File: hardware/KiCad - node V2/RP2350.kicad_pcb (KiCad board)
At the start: 4 copper layers, 56 x 32 mm, 82 parts, among them J3 USB_C_Receptacle_USB2.0_14P, SW1 BOOTSEL, U1 RP2350A, U2 THVD1450D, U3 ADXL355BEZ, U4 TPS2121RUXR, U5 USBLC6-2SC6, U6 TLV75733PDBV, U7 W25Q128JVS, U8 TPS7A20xxxDBV

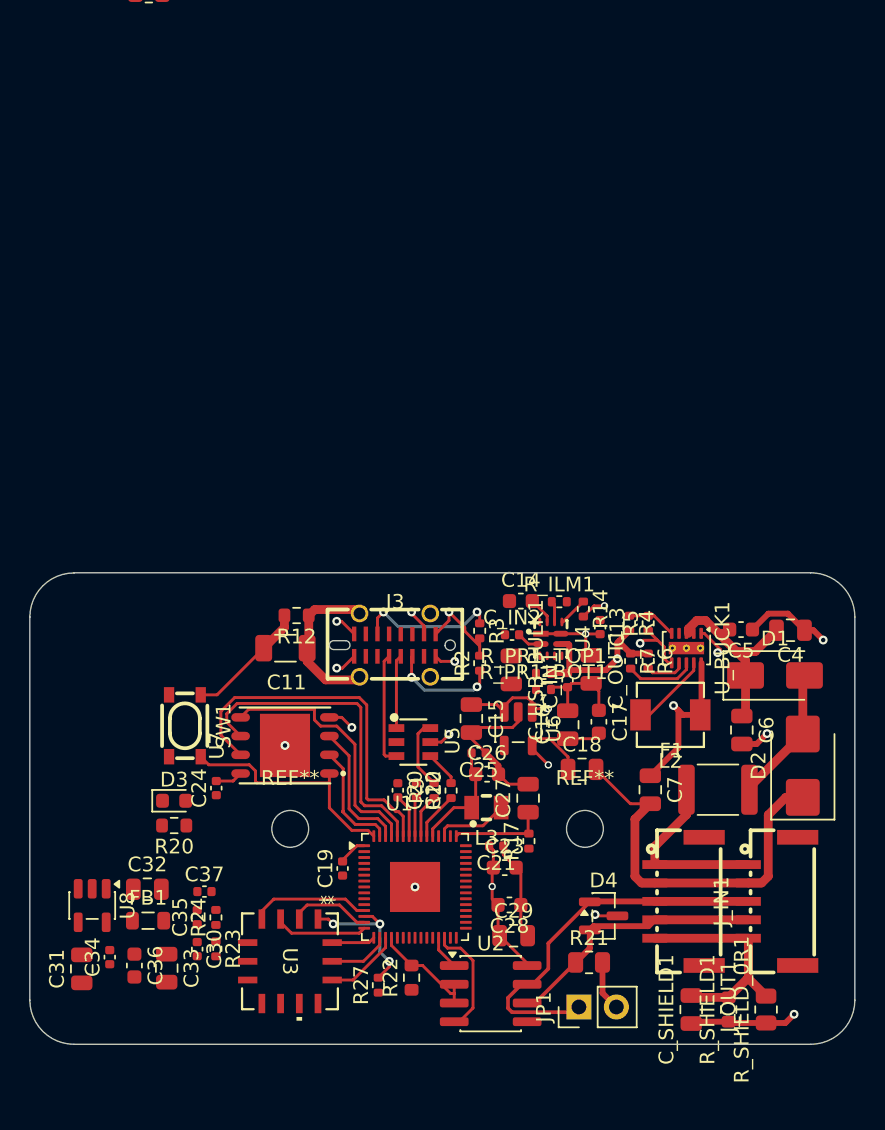
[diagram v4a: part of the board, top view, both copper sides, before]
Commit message: hardware: pico pin change, moved mounting holes
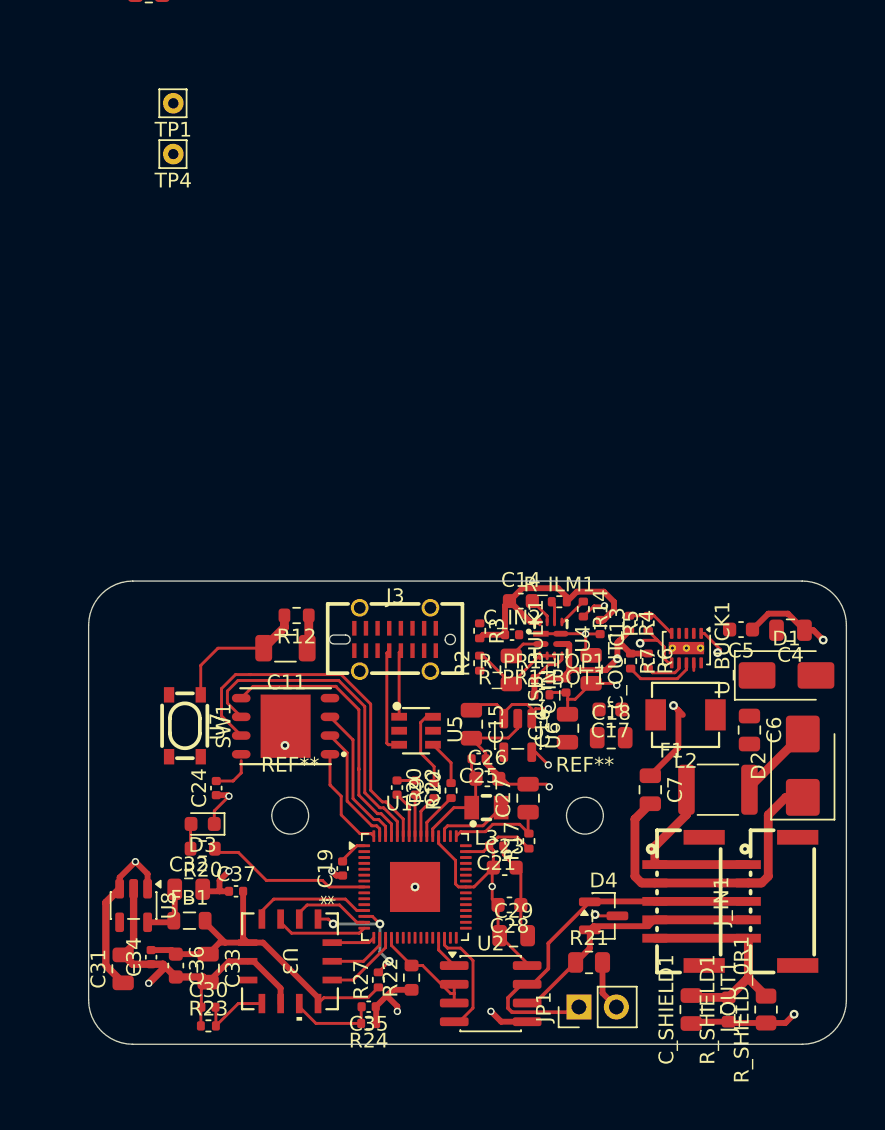
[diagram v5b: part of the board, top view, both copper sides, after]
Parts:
- added TP1: 5V_SYS, Connector_Pin:Pin_D0.7mm_L6.5mm_W1.8mm_FlatFork, F.Cu at (128.3, 45.7)
- added TP4: 12V_Protected, Connector_Pin:Pin_D0.7mm_L6.5mm_W1.8mm_FlatFork, F.Cu at (128.3, 49.1)
- moved C35 13.1 mm to (141.6, 107.0), turned to 180 degrees
- moved R24 12.6 mm to (141.6, 108.1), turned to 180 degrees
- moved R23 5.26 mm to (130.7, 108.3), turned to 0 degrees
- moved C30 4.01 mm to (130.7, 107.0), turned to 0 degrees
- moved C18 2.92 mm to (158.0, 88.7)
- moved C31 2.81 mm to (124.9, 104.4)
- moved C34 2.81 mm to (126.8, 103.6)
- moved FB1 2.81 mm to (129.4, 101.2)
- moved U8 2.81 mm to (125.6, 100.1)
- moved C32 2.81 mm to (129.3, 99.0)
- moved C33 2.81 mm to (130.7, 104.4)
- moved C36 2.81 mm to (128.5, 104.2)
- moved D3 2.50 mm to (130.3, 94.6), turned to 180 degrees
- moved R20 2.50 mm to (130.3, 96.3)
- moved C37 2.14 mm to (132.6, 99.2)
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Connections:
- net /12V_BUS renamed /12V
- net Net-(U1-QSPI_SD1) renamed /DO
- net Net-(U1-QSPI_SD2) renamed /WP
- net Net-(U1-USB_DM) renamed /USB_DM
- net Net-(U1-USB_DP) renamed /USB_DP
- net Net-(U1-~{QSPI_SS}) renamed /CS
- R20 pad 1: Net-(U1-GPIO25) -> Net-(U1-GPIO5)
- R22 pad 2: Net-(U1-GPIO15) -> Net-(U1-GPIO18)
- U1 pad 19: Net-(U1-GPIO15) -> unconnected-(U1-GPIO15-Pad19)
- U1 pad 29: unconnected-(U1-GPIO18-Pad29) -> Net-(U1-GPIO18)
- U1 pad 37: Net-(U1-GPIO25) -> unconnected-(U1-GPIO25-Pad37)
- U1 pad 8: unconnected-(U1-GPIO5-Pad8) -> Net-(U1-GPIO5)
- U2 pad 2: Net-(U1-GPIO15) -> Net-(U1-GPIO18)
- U2 pad 3: Net-(U1-GPIO15) -> Net-(U1-GPIO18)
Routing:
- net /5V_SYS: track 18.7 -> 78.3 mm, vias 2 -> 3
- net GND: track 94.1 -> 141.8 mm, vias 13 -> 15
- net /3V3_ADXL: track 0.00 -> 23.9 mm
- net /3V3_DIG: track 39.5 -> 57.3 mm
- net Net-(D1-K): track 14.1 -> 0.00 mm
- net Net-(U1-GPIO5): track 0.00 -> 11.2 mm
- net Net-(J3-CC2): track 9.68 -> 0.00 mm, vias 2 -> 0
- net Net-(J3-SHELL): track 11.1 -> 2.26 mm
- net /CS: track 16.0 -> 7.24 mm
- net Net-(J3-CC1): track 7.51 -> 0.00 mm, vias 2 -> 0
- net Net-(U1-GPIO15): track 7.40 -> 0.00 mm
- net (no net): track 0.00 -> 7.40 mm
- net Net-(U3-V1P8ANA): track 0.00 -> 6.03 mm
- net Net-(U3-V1P8DIG): track 0.00 -> 5.03 mm
- net Net-(U_BUCK1-SW): track 5.39 -> 0.52 mm
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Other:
- board size 56 x 32 mm -> 51.4 x 31.4 mm

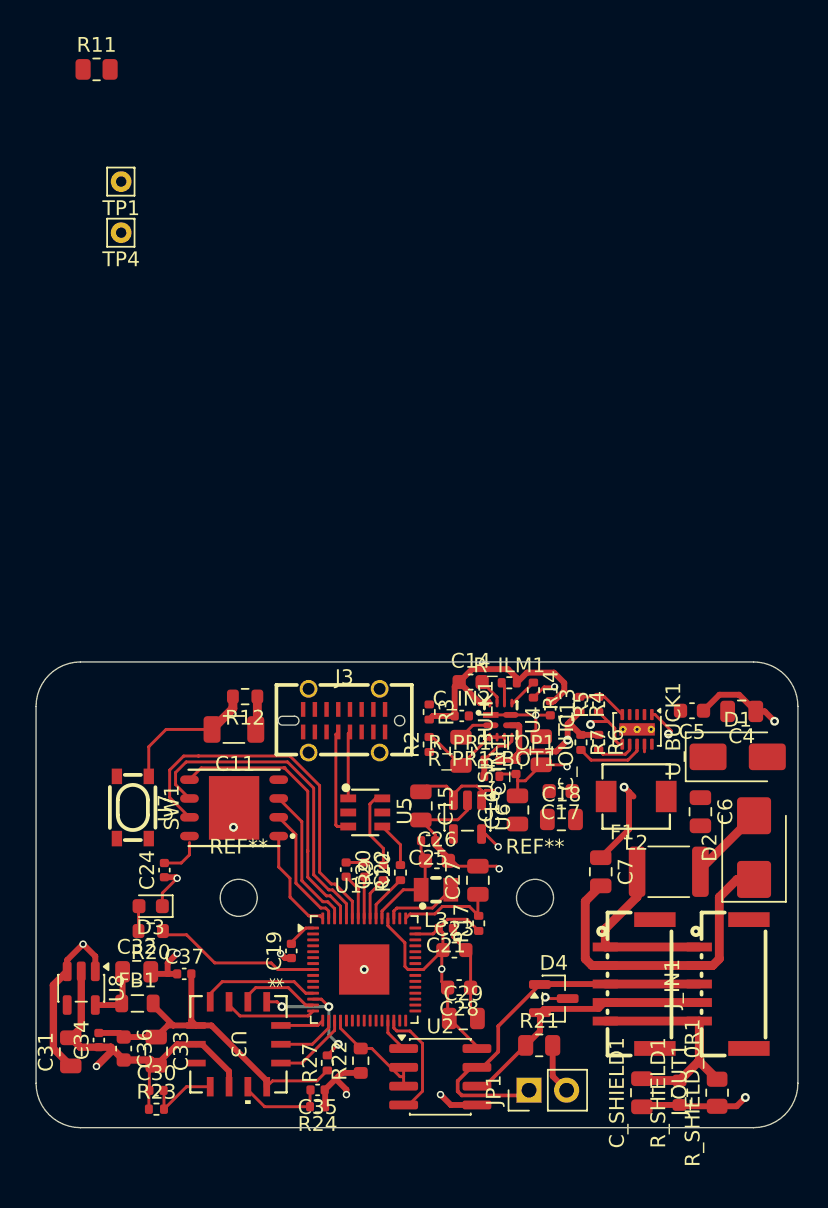
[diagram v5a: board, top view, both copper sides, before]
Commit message: hardware: added footprints, part numbers, layout update
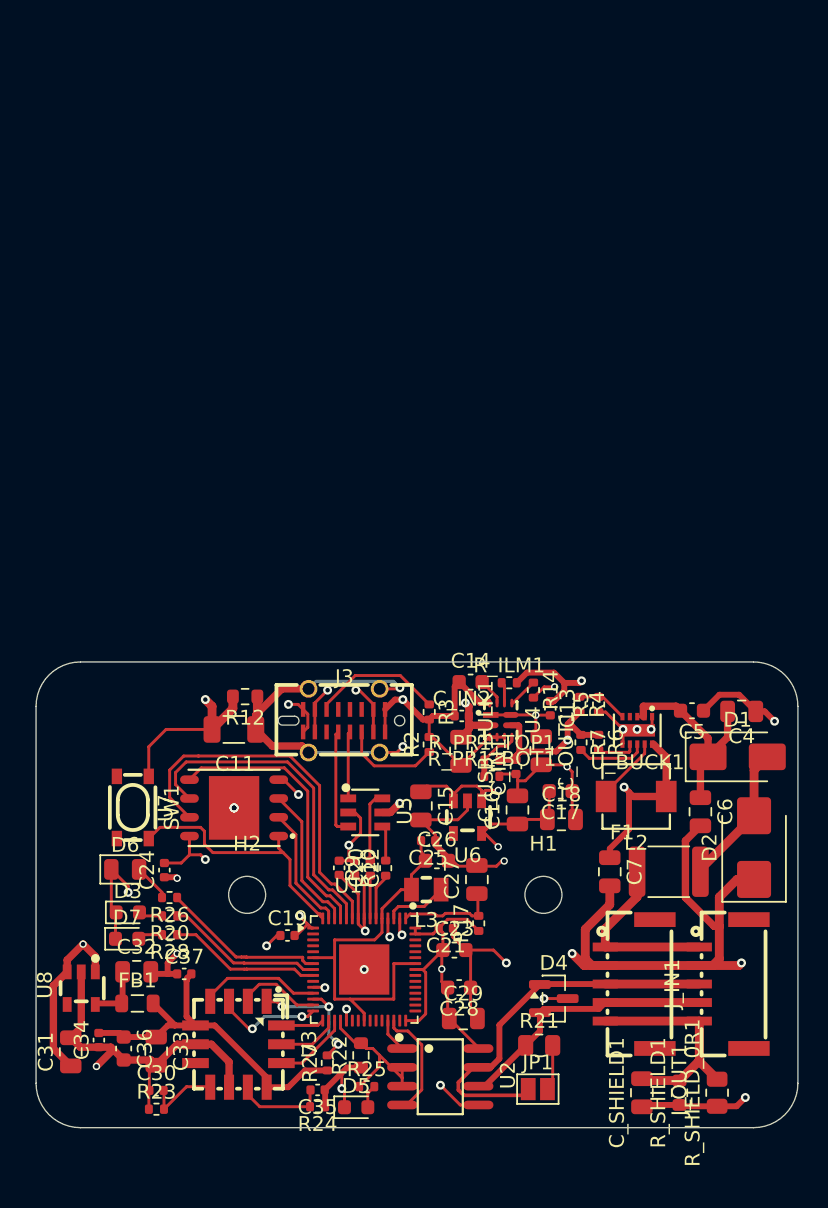
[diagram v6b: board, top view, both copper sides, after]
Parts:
- removed R11: 0 DNP, Resistor_SMD:R_0805_2012Metric
- removed REF** (x2): MountingHole_2.5mm, MountingHole:MountingHole_2.5mm
- removed TP1: 5V_SYS, Connector_Pin:Pin_D0.7mm_L6.5mm_W1.8mm_FlatFork
- removed TP4: 12V_Protected, Connector_Pin:Pin_D0.7mm_L6.5mm_W1.8mm_FlatFork
- added D5: LED_RED, LED_SMD:LED_0603_1608Metric, F.Cu at (144.2, 108.2)
- added D6: LED_GREEN, LED_SMD:LED_0805_2012Metric, F.Cu at (128.6, 92.1)
- added D7: LED_RED, LED_SMD:LED_0603_1608Metric, F.Cu at (128.7, 96.8)
- added H1: MountingHole, MountingHole:MountingHole_2.5mm, F.Cu at (156.8, 93.8)
- added H2: MountingHole, MountingHole:MountingHole_2.5mm, F.Cu at (136.8, 93.8)
- added R25: 2.2k, Resistor_SMD:R_0402_1005Metric, F.Cu at (144.9, 106.8)
- added R26: 2.2k, Resistor_SMD:R_0402_1005Metric, F.Cu at (131.6, 94.0)
- added R28: 2.2k, Resistor_SMD:R_0402_1005Metric, F.Cu at (131.6, 96.5)
- D1: value SS14-E3/61T -> SS14
- D3: value LED -> LED_RED
- JP1: footprint my_footprints:PinHeader_1x02_P2.54mm_Vertical -> Jumper:SolderJumper-2_P1.3mm_Open_Pad1.0x1.5mm
- R20: footprint Resistor_SMD:R_0603_1608Metric -> Resistor_SMD:R_0402_1005Metric
- U2: value THVD1450D -> THVD1450DR; footprint Package_SO:SOIC-8_3.9x4.9mm_P1.27mm -> footprints:THVD1450DR-SOIC-8_L4.9-W3.9-P1.27-LS6.0-BL
- U3: value ADXL355BEZ -> ADXL355BEZ-RL7; footprint my_footprints:E-14-1_ADI-M -> footprints:ADXL355BEZ-RL7
- U6: value TLV75733PDBV -> TLV75733PDBVR; footprint Package_TO_SOT_SMD:SOT-23-5 -> footprints:TLV75733PDBVR-SOT-23-5_L2.9-W1.6-P0.95-LS2.8-BL
- U8: value TPS7A20xxxDBV -> TPS7A2033PDBVR; footprint Package_TO_SOT_SMD:SOT-23-5 -> footprints:TPS7A2033PDBVR
- U_BUCK1: value TPS62175DQC -> TPS62175DQCR; footprint Package_SON:WSON-10-1EP_2x3mm_P0.5mm_EP0.84x2.4mm_ThermalVias -> footprints:TPS62175DQCR_WSON-10_L3.0-W2.0-P0.50-BL-EP
- moved R20 1.64 mm to (131.6, 95.2)
- moved D3 1.60 mm to (128.8, 95.0), turned to 0 degrees
- moved C19 1.08 mm to (139.5, 96.6), turned to 0 degrees
- moved R10 1.04 mm to (146.2, 92.0)
- moved R9 0.93 mm to (145.1, 92.0)
- moved C22 0.68 mm to (144.1, 92.0)
- moved L3 0.65 mm to (148.9, 93.5)
- moved C7 0.61 mm to (161.3, 92.3)
- moved JP1 0.60 mm to (156.4, 106.9), turned to 0 degrees
- moved C20 0.48 mm to (143.0, 92.0)
- moved R22 0.36 mm to (144.5, 104.7)
- moved C27 0.08 mm to (152.3, 92.8)
- moved U_BUCK1 0.07 mm to (163.1, 82.7), turned to 180 degrees
- turned U2 to -90 degrees
- turned U6 to 180 degrees
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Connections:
- R22 pad 2: Net-(U1-GPIO18) -> Net-(U1-GPIO15)
- U1 pad 19: unconnected-(U1-GPIO15-Pad19) -> Net-(U1-GPIO15)
- U1 pad 29: Net-(U1-GPIO18) -> unconnected-(U1-GPIO18-Pad29)
- U1 pad 7: unconnected-(U1-GPIO4-Pad7) -> Net-(U1-GPIO4)
- U1 pad 9: unconnected-(U1-GPIO6-Pad9) -> Net-(U1-GPIO6)
- U2 pad 2: Net-(U1-GPIO18) -> Net-(U1-GPIO15)
- U2 pad 3: Net-(U1-GPIO18) -> Net-(U1-GPIO15)
- U_BUCK1 pad 11: unconnected-(U_BUCK1-PAD-Pad11)_4 -> GND
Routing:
- net GND: track 141.8 -> 182.9 mm, vias 15 -> 29
- net /USB_VBUS: track 2.35 -> 31.6 mm, vias 0 -> 4
- net /3V3_DIG: track 57.3 -> 85.6 mm, vias 3 -> 9
- net Net-(J3-SHELL): track 2.26 -> 28.0 mm, vias 0 -> 2
- net /1V1_CORE: track 7.29 -> 26.5 mm
- net Net-(D1-K): track 0.00 -> 14.3 mm
- net Net-(U1-GPIO4): track 0.00 -> 11.2 mm
- net Net-(U1-GPIO6): track 0.00 -> 10.3 mm
- net /CS: track 7.24 -> 17.5 mm
- net Net-(U1-GPIO15): track 0.00 -> 10.1 mm
- net Net-(J3-CC2): track 0.00 -> 8.89 mm
- net (no net): track 7.40 -> 0.00 mm
- net Net-(J3-CC1): track 0.00 -> 6.74 mm
- net /5V_BUCK: track 23.9 -> 29.7 mm
- net Net-(D1-A): track 5.28 -> 9.63 mm
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- added copper zone on In2.Cu, net /3V3_DIG
- added copper zone on In1.Cu, net GND
